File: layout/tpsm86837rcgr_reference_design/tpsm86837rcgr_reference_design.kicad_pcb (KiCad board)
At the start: 2 copper layers, 16 parts

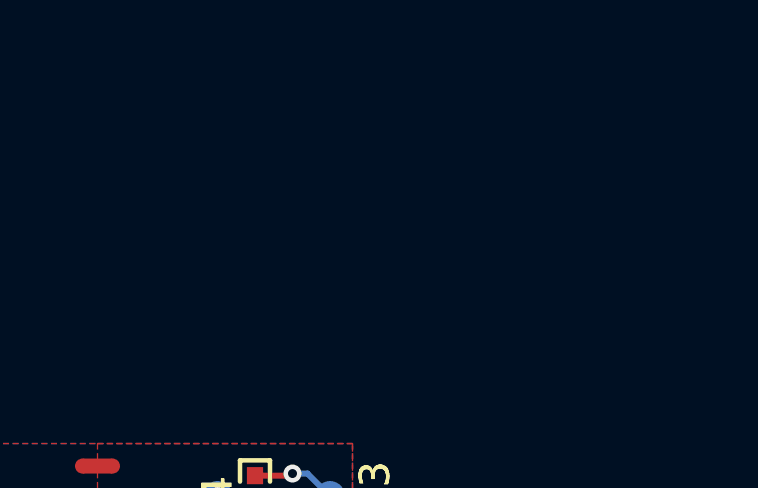
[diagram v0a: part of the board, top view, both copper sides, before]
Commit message: Make UVLO compile
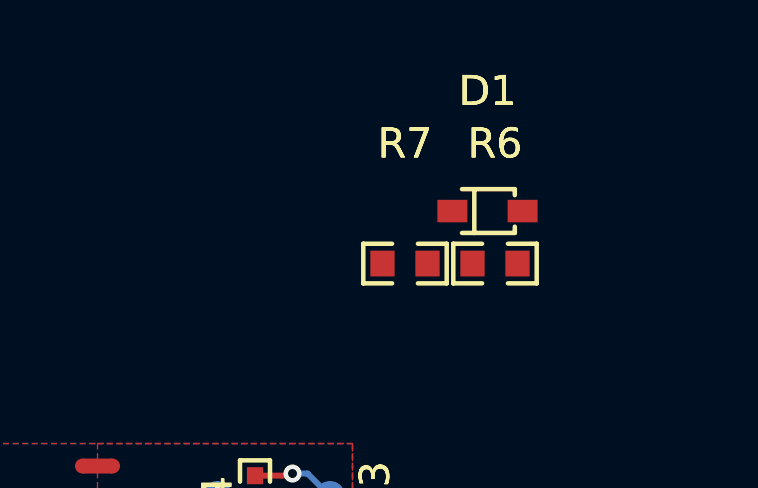
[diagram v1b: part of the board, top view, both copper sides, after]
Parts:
- added D1: , atopile:SOD-323_L1.8-W1.3-LS2.5-RD-b55baa, F.Cu at (8.75, -19.5)
- added R6: 1kΩ ±1% 100mW, atopile:R0603-ebcab9, F.Cu at (9.00, -17.8)
- added R7: 10kΩ ±1% 100mW, atopile:R0603-ebcab9, F.Cu at (6.00, -17.8)
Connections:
- net power_module.footprint.pins[3].net-net renamed net
- C6 pad 1: line-1 -> line-2
- C6 pad 2: output_voltage_feedback-contact-1 -> output_voltage_feedback-contact
- R1 pad 1: line-2 -> line-1
- R2 pad 1: line-1 -> line-2
- R3 pad 1: output_voltage_feedback-contact -> output_voltage_feedback-contact-1
- R3 pad 2: output_voltage_feedback-contact-1 -> output_voltage_feedback-contact
- R4 pad 1: output_voltage_feedback-contact-1 -> output_voltage_feedback-contact
- R4 pad 2: line-1 -> line-2
- TP1 pad 1: output_voltage_feedback-contact -> output_voltage_feedback-contact-1
- TP2 pad 1: output_voltage_feedback-contact-1 -> output_voltage_feedback-contact
- U1 pad 10: power_module.footprint.pins[1].net-net -> switching_node
- U1 pad 11: power_module.footprint.pins[2].net-net -> switching_node
- U1 pad 4: line-1 -> line-2
- U1 pad 6: line-2 -> line-1
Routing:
- net output_voltage_feedback-contact-1: track 4.19 -> 7.77 mm, vias 1 -> 2
- net output_voltage_feedback-contact: track 7.77 -> 4.19 mm, vias 2 -> 1
- net line-2: track 5.14 -> 6.61 mm
- net line-1: track 6.61 -> 5.14 mm
- net hv-2: vias 24 -> 0
- net (no net): vias 0 -> 24
- added copper zone on B.Cu, net (none)
- added copper zone on F.Cu, net (none)
- removed copper zone on B.Cu, net hv-2
- removed copper zone on F.Cu, net hv-2
